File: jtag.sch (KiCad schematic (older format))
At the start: 7 parts, among them J4 NC

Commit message: Use "Start to sheet number*100 and use first free number" designation, any new component added to the schematic will occupy the next available number in that sheet
For example: if sheet 2 has R201-R215 and we add a new resistor it will become R216.
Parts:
- renumbered D10 to D801, J4 to J801, R57 to R801, R58 to R802, R59 to R803, R60 to R804, R61 to R805
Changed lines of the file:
@@
 $EndDescr
 $Comp
-L Conn_02x05_Odd_Even J4
+L Conn_02x05_Odd_Even J801
 U 1 1 5AD052A0
 P 6200 3450
-F 0 "J4" H 6250 3750 50  0000 C CNN
+F 0 "J801" H 6250 3750 50  0000 C CNN
 F 1 "NC" H 6250 3150 50  0000 C CNN
 F 2 "" H 6200 3450 50  0001 C CNN
@@
 $EndComp
 $Comp
-L R R60
+L R R804
 U 1 1 5AD052F0
 P 6750 3550
-F 0 "R60" V 6800 3750 50  0000 C CNN
+F 0 "R804" V 6800 3750 50  0000 C CNN
 F 1 "NC" V 6750 3550 50  0000 C CNN
 F 2 "" V 6680 3550 50  0001 C CNN
@@
 $EndComp
 $Comp
-L R R61
+L R R805
 U 1 1 5AD0530D
 P 6750 3650
-F 0 "R61" V 6830 3650 50  0000 C CNN
+F 0 "R805" V 6830 3650 50  0000 C CNN
 F 1 "0" V 6750 3650 50  0000 C CNN
 F 2 "" V 6680 3650 50  0001 C CNN
@@
 $EndComp
 $Comp
-L R R58
+L R R802
 U 1 1 5AD058A3
 P 6150 3850
-F 0 "R58" V 6230 3850 50  0000 C CNN
+F 0 "R802" V 6230 3850 50  0000 C CNN
 F 1 "NC" V 6150 3850 50  0000 C CNN
 F 2 "" V 6080 3850 50  0001 C CNN
@@
 $EndComp
 $Comp
-L D_Schottky D10
+L D_Schottky D801
 U 1 1 5AD05906
 P 5550 3650
-F 0 "D10" H 5550 3750 50  0000 C CNN
+F 0 "D801" H 5550 3750 50  0000 C CNN
 F 1 "CFSH05-20L" H 5875 3600 50  0000 C CNN
 F 2 "" H 5550 3650 50  0001 C CNN
@@
 $EndComp
 $Comp
-L R R59
+L R R803
 U 1 1 5AD0593B
 P 6450 3050
-F 0 "R59" H 6325 3000 50  0000 C CNN
+F 0 "R803" H 6325 3000 50  0000 C CNN
 F 1 "120" H 6325 3100 50  0000 C CNN
 F 2 "" V 6380 3050 50  0001 C CNN
@@
 $EndComp
 $Comp
-L SOM_NVCC_3V3 #PWR0118
+L SOM_NVCC_3V3 #PWR802
 U 1 1 5AD06892
 P 6450 2850
-F 0 "#PWR0118" H 6450 2700 50  0001 C CNN
+F 0 "#PWR802" H 6450 2700 50  0001 C CNN
 F 1 "SOM_NVCC_3V3" H 6450 2990 50  0000 C CNN
 F 2 "" H 6450 2850 50  0001 C CNN
@@
 Connection ~ 6550 3650
 $Comp
-L GND #PWR0119
+L GND #PWR803
 U 1 1 5AD06B94
 P 6950 3700
-F 0 "#PWR0119" H 6950 3450 50  0001 C CNN
+F 0 "#PWR803" H 6950 3450 50  0001 C CNN
 F 1 "GND" H 6950 3550 50  0000 C CNN
 F 2 "" H 6950 3700 50  0001 C CNN
@@
 Connection ~ 6950 3650
 $Comp
-L R R57
+L R R801
 U 1 1 5AD07568
 P 5750 4050
-F 0 "R57" H 5875 4100 50  0000 C CNN
+F 0 "R801" H 5875 4100 50  0000 C CNN
 F 1 "10k" H 5875 4000 50  0000 C CNN
 F 2 "" V 5680 4050 50  0001 C CNN
@@
 	5750 3350 5750 3900
 $Comp
-L GND #PWR0120
+L GND #PWR801
 U 1 1 5AD075E7
 P 5750 4250
-F 0 "#PWR0120" H 5750 4000 50  0001 C CNN
+F 0 "#PWR801" H 5750 4000 50  0001 C CNN
 F 1 "GND" H 5750 4100 50  0000 C CNN
 F 2 "" H 5750 4250 50  0001 C CNN

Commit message: Move reference designators in the schematic so that they are legible
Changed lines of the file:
@@
 $EndComp
 $Comp
-L SOM_NVCC_3V3 #PWR802
+L SOM_NVCC_3V3 #PWR0118
 U 1 1 5AD06892
 P 6450 2850
-F 0 "#PWR802" H 6450 2700 50  0001 C CNN
+F 0 "#PWR0118" H 6450 2700 50  0001 C CNN
 F 1 "SOM_NVCC_3V3" H 6450 2990 50  0000 C CNN
 F 2 "" H 6450 2850 50  0001 C CNN
@@
 Connection ~ 6550 3650
 $Comp
-L GND #PWR803
+L GND #PWR0119
 U 1 1 5AD06B94
 P 6950 3700
-F 0 "#PWR803" H 6950 3450 50  0001 C CNN
+F 0 "#PWR0119" H 6950 3450 50  0001 C CNN
 F 1 "GND" H 6950 3550 50  0000 C CNN
 F 2 "" H 6950 3700 50  0001 C CNN
@@
 U 1 1 5AD07568
 P 5750 4050
-F 0 "R801" H 5875 4100 50  0000 C CNN
+F 0 "R801" H 5900 4100 50  0000 C CNN
 F 1 "10k" H 5875 4000 50  0000 C CNN
 F 2 "" V 5680 4050 50  0001 C CNN
@@
 	5750 3350 5750 3900
 $Comp
-L GND #PWR801
+L GND #PWR0120
 U 1 1 5AD075E7
 P 5750 4250
-F 0 "#PWR801" H 5750 4000 50  0001 C CNN
+F 0 "#PWR0120" H 5750 4000 50  0001 C CNN
 F 1 "GND" H 5750 4100 50  0000 C CNN
 F 2 "" H 5750 4250 50  0001 C CNN

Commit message: Include reverse polarity protection circuit along with a simulation showing its effectiveness
Protecting VBAT from when board is sinking current via USB C. Protects against reverse polarity at the DC jack.

In EmCraft's instance VBUS should only be 5V when sinking current but they must protect against the condition when VBUS>12V and DC_IN=12V. This may need testing.
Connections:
- net labels added: 3V3_OUT
- net labels removed: SOM_NVCC_3V3
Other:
- note added: "ARM DStream"
- moved on the sheet: D801, J801, R801, R802, R803, R804, R805
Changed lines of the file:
@@
 Sheet 8 14
 Title "JTAG"
-Date "2018-04-16"
+Date "2018-04-18"
 Rev "v0.1.0"
 Comp "Purism SPC"
@@
 L Conn_02x05_Odd_Even J801
 U 1 1 5AD052A0
-P 6200 3450
-F 0 "J801" H 6250 3750 50  0000 C CNN
-F 1 "NC" H 6250 3150 50  0000 C CNN
-F 2 "" H 6200 3450 50  0001 C CNN
-F 3 "https://media.digikey.com/pdf/Data%20Sheets/Sullins%20PDFs/GRPB_%20_2VWQS-RC%2010958-C.pdf" H 6200 3450 50  0001 C CNN
-F 4 "Sullins" H 6200 3450 60  0001 C CNN "MFG Name"
-F 5 "GRPB052VWQS-RC" H 6200 3450 60  0001 C CNN "MFG Part Num"
-F 6 "S9012E-05-ND" H 6200 3450 60  0001 C CNN "Distrib PN"
-F 7 "https://www.digikey.com/product-detail/en/sullins-connector-solutions/GRPB052VWQS-RC/S9012E-05-ND/1786414" H 6200 3450 60  0001 C CNN "Distrib Link"
-F 8 "-" H 6200 3450 60  0001 C CNN "Tolerance"
-F 9 "https://www.digikey.com/products/en/connectors-interconnects/rectangular-connectors-headers-male-pins/314?k=&pkeyword=&pv2024=6&FV=1140003%2C160000a%2C1680002%2C1fa40016%2Cffe0013a&quantity=0&ColumnSort=1000011&page=1&pageSize=500" H 6200 3450 60  0001 C CNN "Others"
-	1    6200 3450
+P 6150 3550
+F 0 "J801" H 6200 3850 50  0000 C CNN
+F 1 "NC" H 6200 3250 50  0000 C CNN
+F 2 "" H 6150 3550 50  0001 C CNN
+F 3 "https://media.digikey.com/pdf/Data%20Sheets/Sullins%20PDFs/GRPB_%20_2VWQS-RC%2010958-C.pdf" H 6150 3550 50  0001 C CNN
+F 4 "Sullins" H 6150 3550 60  0001 C CNN "MFG Name"
+F 5 "GRPB052VWQS-RC" H 6150 3550 60  0001 C CNN "MFG Part Num"
+F 6 "S9012E-05-ND" H 6150 3550 60  0001 C CNN "Distrib PN"
+F 7 "https://www.digikey.com/product-detail/en/sullins-connector-solutions/GRPB052VWQS-RC/S9012E-05-ND/1786414" H 6150 3550 60  0001 C CNN "Distrib Link"
+F 8 "-" H 6150 3550 60  0001 C CNN "Tolerance"
+F 9 "https://www.digikey.com/products/en/connectors-interconnects/rectangular-connectors-headers-male-pins/314?k=&pkeyword=&pv2024=6&FV=1140003%2C160000a%2C1680002%2C1fa40016%2Cffe0013a&quantity=0&ColumnSort=1000011&page=1&pageSize=500" H 6150 3550 60  0001 C CNN "Others"
+	1    6150 3550
 	-1   0    0    -1
 $EndComp
@@
 L R R804
 U 1 1 5AD052F0
-P 6750 3550
-F 0 "R804" V 6800 3750 50  0000 C CNN
-F 1 "NC" V 6750 3550 50  0000 C CNN
-F 2 "" V 6680 3550 50  0001 C CNN
-F 3 "" H 6750 3550 50  0001 C CNN
-	1    6750 3550
+P 6700 3650
+F 0 "R804" V 6750 3850 50  0000 C CNN
+F 1 "NC" V 6700 3650 50  0000 C CNN
+F 2 "" V 6630 3650 50  0001 C CNN
+F 3 "" H 6700 3650 50  0001 C CNN
+	1    6700 3650
 	0    -1   -1   0
 $EndComp
@@
 L R R805
 U 1 1 5AD0530D
-P 6750 3650
-F 0 "R805" V 6830 3650 50  0000 C CNN
-F 1 "0" V 6750 3650 50  0000 C CNN
-F 2 "" V 6680 3650 50  0001 C CNN
-F 3 "" H 6750 3650 50  0001 C CNN
-	1    6750 3650
+P 6700 3750
+F 0 "R805" V 6780 3750 50  0000 C CNN
+F 1 "0" V 6700 3750 50  0000 C CNN
+F 2 "" V 6630 3750 50  0001 C CNN
+F 3 "" H 6700 3750 50  0001 C CNN
+	1    6700 3750
 	0    1    1    0
 $EndComp
@@
 L R R802
 U 1 1 5AD058A3
-P 6150 3850
-F 0 "R802" V 6230 3850 50  0000 C CNN
-F 1 "NC" V 6150 3850 50  0000 C CNN
-F 2 "" V 6080 3850 50  0001 C CNN
-F 3 "" H 6150 3850 50  0001 C CNN
-	1    6150 3850
+P 6100 3950
+F 0 "R802" V 6180 3950 50  0000 C CNN
+F 1 "NC" V 6100 3950 50  0000 C CNN
+F 2 "" V 6030 3950 50  0001 C CNN
+F 3 "" H 6100 3950 50  0001 C CNN
+	1    6100 3950
 	0    1    1    0
 $EndComp
@@
 L D_Schottky D801
 U 1 1 5AD05906
-P 5550 3650
-F 0 "D801" H 5550 3750 50  0000 C CNN
-F 1 "CFSH05-20L" H 5875 3600 50  0000 C CNN
-F 2 "" H 5550 3650 50  0001 C CNN
-F 3 "" H 5550 3650 50  0001 C CNN
-	1    5550 3650
+P 5500 3750
+F 0 "D801" H 5500 3850 50  0000 C CNN
+F 1 "CFSH05-20L" H 5825 3700 50  0000 C CNN
+F 2 "" H 5500 3750 50  0001 C CNN
+F 3 "" H 5500 3750 50  0001 C CNN
+	1    5500 3750
 	-1   0    0    1
 $EndComp
@@
 L R R803
 U 1 1 5AD0593B
-P 6450 3050
-F 0 "R803" H 6325 3000 50  0000 C CNN
-F 1 "120" H 6325 3100 50  0000 C CNN
-F 2 "" V 6380 3050 50  0001 C CNN
-F 3 "" H 6450 3050 50  0001 C CNN
-	1    6450 3050
+P 6400 3150
+F 0 "R803" H 6250 3100 50  0000 C CNN
+F 1 "120" H 6275 3200 50  0000 C CNN
+F 2 "" V 6330 3150 50  0001 C CNN
+F 3 "" H 6400 3150 50  0001 C CNN
+	1    6400 3150
 	-1   0    0    1
 $EndComp
-$Comp
-L SOM_NVCC_3V3 #PWR0118
-U 1 1 5AD06892
-P 6450 2850
-F 0 "#PWR0118" H 6450 2700 50  0001 C CNN
-F 1 "SOM_NVCC_3V3" H 6450 2990 50  0000 C CNN
-F 2 "" H 6450 2850 50  0001 C CNN
-F 3 "" H 6450 2850 50  0001 C CNN
-	1    6450 2850
-	1    0    0    -1
-$EndComp
-Wire Wire Line
-	6400 3250 6450 3250
-Wire Wire Line
-	6450 3250 6450 3200
-Wire Wire Line
-	6450 2900 6450 2850
-Wire Wire Line
-	6400 3550 6600 3550
-Wire Wire Line
-	6400 3650 6600 3650
-Wire Wire Line
-	6300 3850 6550 3850
-Wire Wire Line
-	6550 3850 6550 3650
-Connection ~ 6550 3650
-$Comp
-L GND #PWR0119
+Wire Wire Line
+	6350 3350 6400 3350
+Wire Wire Line
+	6400 3350 6400 3300
+Wire Wire Line
+	6400 3000 6400 2950
+Wire Wire Line
+	6350 3650 6550 3650
+Wire Wire Line
+	6350 3750 6550 3750
+Wire Wire Line
+	6250 3950 6500 3950
+Wire Wire Line
+	6500 3950 6500 3750
+Connection ~ 6500 3750
+$Comp
+L GND #PWR0118
 U 1 1 5AD06B94
-P 6950 3700
-F 0 "#PWR0119" H 6950 3450 50  0001 C CNN
-F 1 "GND" H 6950 3550 50  0000 C CNN
-F 2 "" H 6950 3700 50  0001 C CNN
-F 3 "" H 6950 3700 50  0001 C CNN
-	1    6950 3700
-	1    0    0    -1
-$EndComp
-Wire Wire Line
-	6400 3350 6950 3350
-Wire Wire Line
-	6950 3350 6950 3700
-Wire Wire Line
-	6400 3450 6950 3450
-Connection ~ 6950 3450
-Wire Wire Line
-	6900 3550 6950 3550
-Connection ~ 6950 3550
-Wire Wire Line
-	6900 3650 6950 3650
-Connection ~ 6950 3650
+P 6900 3800
+F 0 "#PWR0118" H 6900 3550 50  0001 C CNN
+F 1 "GND" H 6900 3650 50  0000 C CNN
+F 2 "" H 6900 3800 50  0001 C CNN
+F 3 "" H 6900 3800 50  0001 C CNN
+	1    6900 3800
+	1    0    0    -1
+$EndComp
+Wire Wire Line
+	6350 3450 6900 3450
+Wire Wire Line
+	6900 3450 6900 3800
+Wire Wire Line
+	6350 3550 6900 3550
+Connection ~ 6900 3550
+Wire Wire Line
+	6850 3650 6900 3650
+Connection ~ 6900 3650
+Wire Wire Line
+	6850 3750 6900 3750
+Connection ~ 6900 3750
 $Comp
 L R R801
 U 1 1 5AD07568
-P 5750 4050
-F 0 "R801" H 5900 4100 50  0000 C CNN
-F 1 "10k" H 5875 4000 50  0000 C CNN
-F 2 "" V 5680 4050 50  0001 C CNN
-F 3 "" H 5750 4050 50  0001 C CNN
-	1    5750 4050
-	1    0    0    -1
-$EndComp
-Wire Wire Line
-	4550 3350 5900 3350
-Wire Wire Line
-	5750 3350 5750 3900
-$Comp
-L GND #PWR0120
+P 5700 4150
+F 0 "R801" H 5850 4200 50  0000 C CNN
+F 1 "10k" H 5825 4100 50  0000 C CNN
+F 2 "" V 5630 4150 50  0001 C CNN
+F 3 "" H 5700 4150 50  0001 C CNN
+	1    5700 4150
+	1    0    0    -1
+$EndComp
+Wire Wire Line
+	4500 3450 5850 3450
+Wire Wire Line
+	5700 3450 5700 4000
+$Comp
+L GND #PWR0119
 U 1 1 5AD075E7
-P 5750 4250
-F 0 "#PWR0120" H 5750 4000 50  0001 C CNN
-F 1 "GND" H 5750 4100 50  0000 C CNN
-F 2 "" H 5750 4250 50  0001 C CNN
-F 3 "" H 5750 4250 50  0001 C CNN
-	1    5750 4250
-	1    0    0    -1
-$EndComp
-Wire Wire Line
-	5750 4250 5750 4200
-Text HLabel 4550 3250 0    60   Output ~ 0
+P 5700 4350
+F 0 "#PWR0119" H 5700 4100 50  0001 C CNN
+F 1 "GND" H 5700 4200 50  0000 C CNN
+F 2 "" H 5700 4350 50  0001 C CNN
+F 3 "" H 5700 4350 50  0001 C CNN
+	1    5700 4350
+	1    0    0    -1
+$EndComp
+Wire Wire Line
+	5700 4350 5700 4300
+Text HLabel 4500 3350 0    60   Output ~ 0
 JTAG_TMS
-Text HLabel 4550 3350 0    60   Output ~ 0
+Text HLabel 4500 3450 0    60   Output ~ 0
 JTAG_TCK
-Text HLabel 4550 3450 0    60   Input ~ 0
+Text HLabel 4500 3550 0    60   Input ~ 0
 JTAG_TDO
-Text HLabel 4550 3550 0    60   Output ~ 0
+Text HLabel 4500 3650 0    60   Output ~ 0
 JTAG_TDI
-Text HLabel 4550 3650 0    60   Output ~ 0
+Text HLabel 4500 3750 0    60   Output ~ 0
 POR_B
 Wire Wire Line
-	4550 3250 5900 3250
-Connection ~ 5750 3350
-Wire Wire Line
-	4550 3450 5900 3450
-Wire Wire Line
-	4550 3550 5900 3550
-Wire Wire Line
-	4550 3650 5400 3650
-Wire Wire Line
-	5700 3650 5900 3650
-Wire Wire Line
-	6000 3850 4550 3850
-Text HLabel 4550 3850 0    60   Output ~ 0
+	4500 3350 5850 3350
+Connection ~ 5700 3450
+Wire Wire Line
+	4500 3550 5850 3550
+Wire Wire Line
+	4500 3650 5850 3650
+Wire Wire Line
+	4500 3750 5350 3750
+Wire Wire Line
+	5650 3750 5850 3750
+Wire Wire Line
+	5950 3950 4500 3950
+Text HLabel 4500 3950 0    60   Output ~ 0
 JTAG_~TRST
-Text Notes 4600 3250 0    60   ~ 0
+Text Notes 4550 3350 0    60   ~ 0
 90K PD
-Text Notes 4600 3350 0    60   ~ 0
-27K PU
-Text Notes 4600 3450 0    60   ~ 0
-27K PU
-Text Notes 4600 3550 0    60   ~ 0
-27K PU
-Text Notes 4600 3650 0    60   ~ 0
-27K PU
-Text Notes 4600 3850 0    60   ~ 0
-27K PU
-Text Notes 4600 3100 0    60   ~ 0
+Text Notes 4550 3450 0    60   ~ 0
+27K PU
+Text Notes 4550 3550 0    60   ~ 0
+27K PU
+Text Notes 4550 3650 0    60   ~ 0
+27K PU
+Text Notes 4550 3750 0    60   ~ 0
+27K PU
+Text Notes 4550 3950 0    60   ~ 0
+27K PU
+Text Notes 4550 3200 0    60   ~ 0
 Internal
+Text Notes 5700 3200 0    60   ~ 0
+ARM DStream
+$Comp
+L 3V3_OUT #PWR0120
+U 1 1 5AEA3F80
+P 6400 2950
+F 0 "#PWR0120" H 6400 2800 50  0001 C CNN
+F 1 "3V3_OUT" H 6400 3090 50  0000 C CNN
+F 2 "" H 6400 2950 50  0001 C CNN
+F 3 "" H 6400 2950 50  0001 C CNN
+	1    6400 2950
+	1    0    0    -1
+$EndComp
 $EndSCHEMATC

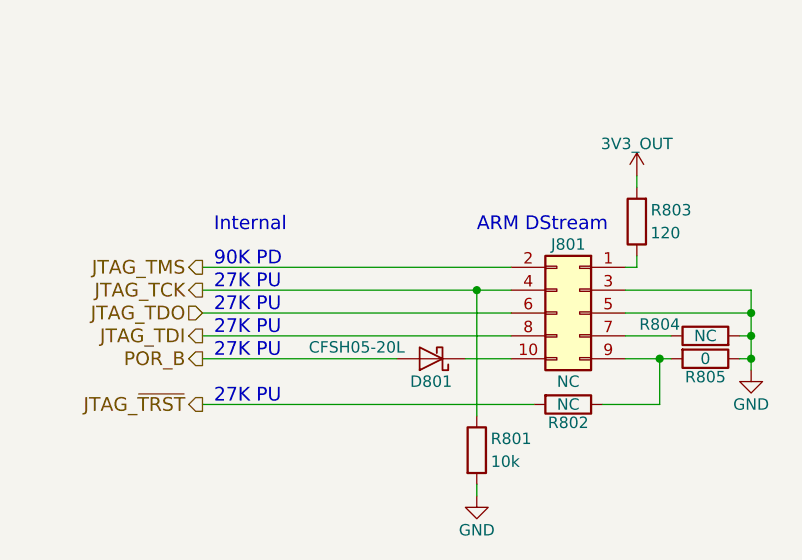
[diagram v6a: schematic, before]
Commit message: Modify the boot config pins such that the eMMC is an 8-bit bus, depressing a momentary push button switch during boot causes SD boot, and relevant options
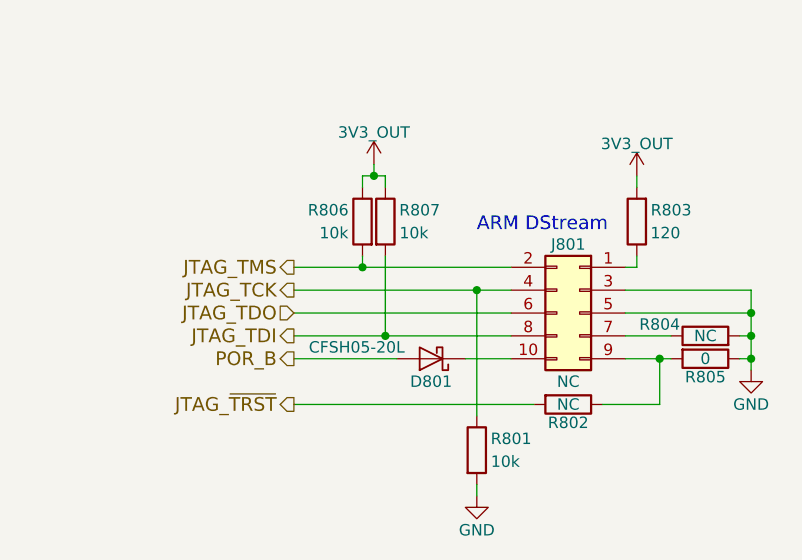
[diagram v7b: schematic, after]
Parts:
- added R806, R807: 10k, symbol R
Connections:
- net 3V3_OUT: now also R806.1, R807.1
- net JTAG_TDI: now also R807.2
- net JTAG_TMS: now also R806.2
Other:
- note removed: "27K PU"
- note removed: "90K PD"
- note removed: "Internal"
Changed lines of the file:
@@
 Connection ~ 6500 3750
 $Comp
-L GND #PWR0119
+L GND #PWR0115
 U 1 1 5AD06B94
 P 6900 3800
-F 0 "#PWR0119" H 6900 3550 50  0001 C CNN
+F 0 "#PWR0115" H 6900 3550 50  0001 C CNN
 F 1 "GND" H 6900 3650 50  0000 C CNN
 F 2 "" H 6900 3800 50  0001 C CNN
@@
 $EndComp
 Wire Wire Line
-	4500 3450 5850 3450
+	4900 3450 5850 3450
 Wire Wire Line
 	5700 3450 5700 4000
 $Comp
-L GND #PWR0120
+L GND #PWR0116
 U 1 1 5AD075E7
 P 5700 4350
-F 0 "#PWR0120" H 5700 4100 50  0001 C CNN
+F 0 "#PWR0116" H 5700 4100 50  0001 C CNN
 F 1 "GND" H 5700 4200 50  0000 C CNN
 F 2 "" H 5700 4350 50  0001 C CNN
@@
 Wire Wire Line
 	5700 4350 5700 4300
-Text HLabel 4500 3350 0    60   Output ~ 0
+Text HLabel 4900 3350 0    60   Output ~ 0
 JTAG_TMS
-Text HLabel 4500 3450 0    60   Output ~ 0
+Text HLabel 4900 3450 0    60   Output ~ 0
 JTAG_TCK
-Text HLabel 4500 3550 0    60   Input ~ 0
+Text HLabel 4900 3550 0    60   Input ~ 0
 JTAG_TDO
-Text HLabel 4500 3650 0    60   Output ~ 0
+Text HLabel 4900 3650 0    60   Output ~ 0
 JTAG_TDI
-Text HLabel 4500 3750 0    60   Output ~ 0
+Text HLabel 4900 3750 0    60   Output ~ 0
 POR_B
 Wire Wire Line
-	4500 3350 5850 3350
+	4900 3350 5850 3350
 Connection ~ 5700 3450
 Wire Wire Line
-	4500 3550 5850 3550
+	4900 3550 5850 3550
 Wire Wire Line
-	4500 3650 5850 3650
+	4900 3650 5850 3650
 Wire Wire Line
-	4500 3750 5350 3750
+	4900 3750 5350 3750
 Wire Wire Line
 	5650 3750 5850 3750
 Wire Wire Line
-	5950 3950 4500 3950
-Text HLabel 4500 3950 0    60   Output ~ 0
+	5950 3950 4900 3950
+Text HLabel 4900 3950 0    60   Output ~ 0
 JTAG_~TRST
-Text Notes 4550 3350 0    60   ~ 0
-90K PD
-Text Notes 4550 3450 0    60   ~ 0
-27K PU
-Text Notes 4550 3550 0    60   ~ 0
-27K PU
-Text Notes 4550 3650 0    60   ~ 0
-27K PU
-Text Notes 4550 3750 0    60   ~ 0
-27K PU
-Text Notes 4550 3950 0    60   ~ 0
-27K PU
-Text Notes 4550 3200 0    60   ~ 0
-Internal
 Text Notes 5700 3200 0    60   ~ 0
 ARM DStream
 $Comp
-L 3V3_OUT #PWR0121
+L 3V3_OUT #PWR0117
 U 1 1 5AEA3F80
 P 6400 2950
-F 0 "#PWR0121" H 6400 2800 50  0001 C CNN
+F 0 "#PWR0117" H 6400 2800 50  0001 C CNN
 F 1 "3V3_OUT" H 6400 3090 50  0000 C CNN
 F 2 "" H 6400 2950 50  0001 C CNN
@@
 	1    0    0    -1
 $EndComp
+$Comp
+L R R806
+U 1 1 5AE57347
+P 5200 3150
+F 0 "R806" H 5350 3200 50  0000 C CNN
+F 1 "10k" H 5325 3100 50  0000 C CNN
+F 2 "" V 5130 3150 50  0001 C CNN
+F 3 "" H 5200 3150 50  0001 C CNN
+	1    5200 3150
+	-1   0    0    -1
+$EndComp
+$Comp
+L R R807
+U 1 1 5AE5736E
+P 5300 3150
+F 0 "R807" H 5450 3200 50  0000 C CNN
+F 1 "10k" H 5425 3100 50  0000 C CNN
+F 2 "" V 5230 3150 50  0001 C CNN
+F 3 "" H 5300 3150 50  0001 C CNN
+	1    5300 3150
+	1    0    0    -1
+$EndComp
+$Comp
+L 3V3_OUT #PWR0118
+U 1 1 5AE5744F
+P 5250 2900
+F 0 "#PWR0118" H 5250 2750 50  0001 C CNN
+F 1 "3V3_OUT" H 5250 3040 50  0000 C CNN
+F 2 "" H 5250 2900 50  0001 C CNN
+F 3 "" H 5250 2900 50  0001 C CNN
+	1    5250 2900
+	1    0    0    -1
+$EndComp
+Wire Wire Line
+	5200 3000 5200 2950
+Wire Wire Line
+	5200 2950 5300 2950
+Wire Wire Line
+	5300 2950 5300 3000
+Wire Wire Line
+	5250 2950 5250 2900
+Connection ~ 5250 2950
+Wire Wire Line
+	5200 3300 5200 3350
+Connection ~ 5200 3350
+Wire Wire Line
+	5300 3300 5300 3650
+Connection ~ 5300 3650
 $EndSCHEMATC
